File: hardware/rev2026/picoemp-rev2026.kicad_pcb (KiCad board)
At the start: 2 copper layers, 40 x 130 mm, 53 parts, among them J1 EDGE-SMA, J2 1x2_Pin_Header, J3 MKDS 1,5/2-5.08, J4 EDGE-SMA, P1 Header 7, P2 Header 2, P3 Header 4, Q1 LDA111STR, Q2 RGT16BM65DTL, Q3 AO3422, Q4 AO3422, SW1 KSC741J LFS, SW2 KSC741J LFS, SW3 TL3301AF160QJ, T1 ATB322524, T2 ATB322524, U1 SC0915, U2 74LVC1G17

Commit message: J3: MKDS -> MKDSN 1,5/2-5,08 for 630 V headroom, with a local footprint
J3 sits across HV_SENSE/HV_RTN at ~246 V on a 300 V-rated MKDS. Phoenix
publishes the MKDSN's rating per IEC 60664-1 category rather than as one number:

  III/3   250 V   clearance 3 mm   creepage 3.2 mm
  III/2   400 V   clearance 3 mm   creepage 3.0 mm
  II/2    630 V   clearance 3 mm   creepage 3.2 mm

This board is USB-powered, mains-isolated and enclosed, which is overvoltage
category II / pollution degree 2 -- so 630 V applies, giving 2.6x margin and
clearing upstream's 400 V barrier design rating. Material group I, CTI 600,
4 kV rated surge, UL94 V0, glow wire 850 C. cULus recognition is 300 V / 10 A
and VDE 400 V / 17.5 A, which are the numbers to quote if a listing is ever
needed.

Chose MKDSN (0 deg entry) over SMKDSN (45 deg). They are electrically
identical; the MKDSN is 10.16 x 8.15 x 13.5 against the SMKDSN's
11.16 x 12 x 14.5. The SMKDSN is larger than the existing courtyard in both
axes and leaves only 0.55 mm under the 1551G shield, versus 1.55 mm for the
MKDSN -- itself better than the 1.25 mm the MKDS had.

New picoemp:TerminalBlock_Phoenix_MKDSN-1,5-2-5.08_1x02_P5.08mm_Horizontal.
Copper is unchanged from the stock MKDS land -- 1.3 mm drill, 2.6 mm pad,
5.08 pitch -- so the pads landed on exactly the same coordinates and nothing
rerouted. Only the outline differs: 8.15 deep rather than 9.8. The datasheet
does not publish where the pins sit within that depth, so the outline keeps the
rear edge where the MKDS had it and pulls the front in by 1.65 mm; that is silk
and courtyard only, noted in the footprint description.

Also corrected J3's schematic Description to carry the real ratings, and
replaced the BOM comment that still claimed a milled slot between the pads --
that slot was never cut, and the 5.08 mm part's 2.480 mm pad separation is the
documented fallback.

DigiKey PN cleared -- the MKDSN needs looking up. bom/ regenerated and J3 now
shows the Phoenix item number 1548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
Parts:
- J3: value MKDS 1,5/2-5.08 -> MKDSN 1,5/2-5,08; footprint TerminalBlock_Phoenix:TerminalBlock_Phoenix_MKDS-1,5-2-5.08_1x02_P5.08mm_Horizontal -> picoemp:TerminalBlock_Phoenix_MKDSN-1,5-2-5.08_1x02_P5.08mm_Horizontal

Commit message: C3 nudge, silk additions, fab outputs regenerated
Alex's work. C3 moved, two more silkscreen objects, three more track objects,
and production/ regenerated including a PicoEMP_2026_A.zip gerber package
alongside the existing one.

Gates: 66 tests pass; DRC exit 0 with warnings included.

Co-Authored-By: Claude Opus 5 <noreply@anthropic.com>
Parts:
- moved C3 0.66 mm to (126.9, 164.7)
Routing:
- net /HV_RTN: track 89.2 -> 90.7 mm
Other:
- board text added: "+"
- board text added: "-"

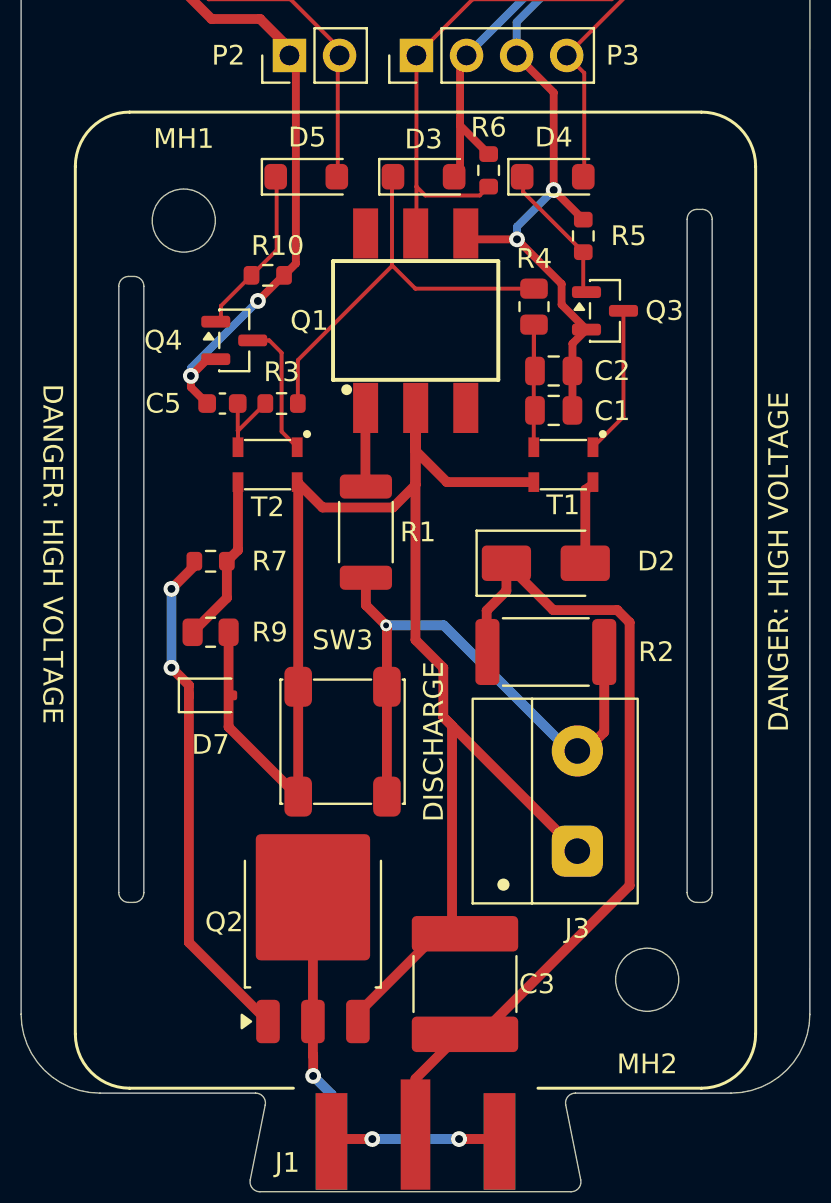
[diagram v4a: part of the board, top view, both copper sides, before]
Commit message: Drop the shield slots; put MH1/MH2 on the correct diagonal
The two 1.27 mm longitudinal slots came from REV04, where they received
the 1551B top half's protruding wall lip and its two locating posts.
Measured off the models: the 1551B top has material down to Z = -2.5,
the 1551G box has zmin = -1e-07 -- a flat rim with nothing below the PCB
face. The slots received nothing, and at centres +/-14.41 mm from board
centre they matched neither shell. No copper crossed either one.

MH1/MH2 were placed from the Hammond model's raw coordinates. The model
is in KiCad's 3D-model frame, where +Y runs opposite to board Y, so the
holes landed on the opposite diagonal from the box bores -- the box would
only have screwed on from the underside. Mapped correctly the bores are
at (136.140, 126.022) and (112.640, 164.522), which is what this file
already documented as (+/-19.25, -/+11.75).

Two conflicts come with the swap and are left open: HV_GATE runs through
MH2, and MH1's courtyard overlaps R5 and D4 (a #4 head clears R5's
nearest pad edge by 0.015 mm). DRC reports those 4 errors and nothing
else; 77 tests pass; 0 unconnected, 0 schematic-parity issues.

Co-Authored-By: Claude Opus 5 <noreply@anthropic.com>
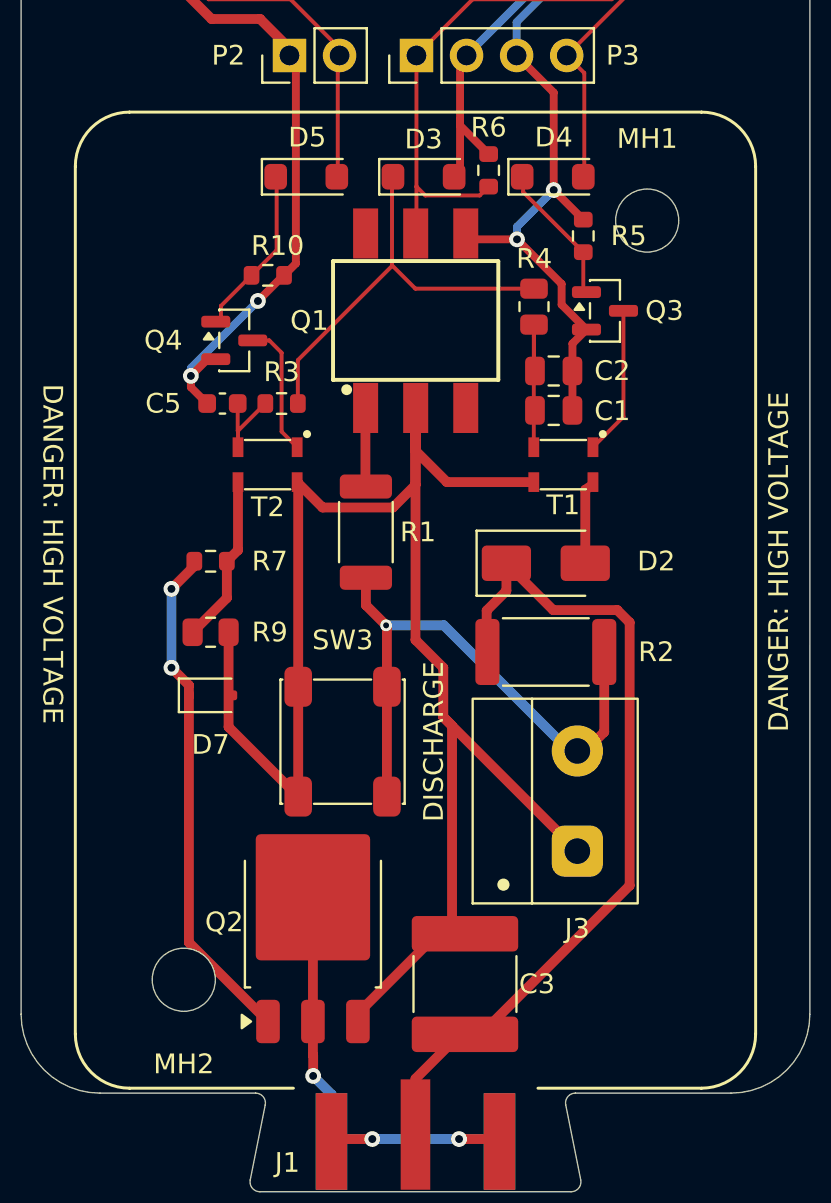
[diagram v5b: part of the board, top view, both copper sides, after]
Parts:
- moved MH1 23.5 mm to (136.1, 126.0)
- moved MH2 23.5 mm to (112.6, 164.5)
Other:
- outline, holes or cut-outs redrawn
